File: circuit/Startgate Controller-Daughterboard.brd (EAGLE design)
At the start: 70 x 90 mm, 14 parts, among them U2 HEF4066BT, U3 HEF4066BT, U4 HEF4066BT, U5 HEF4066BT

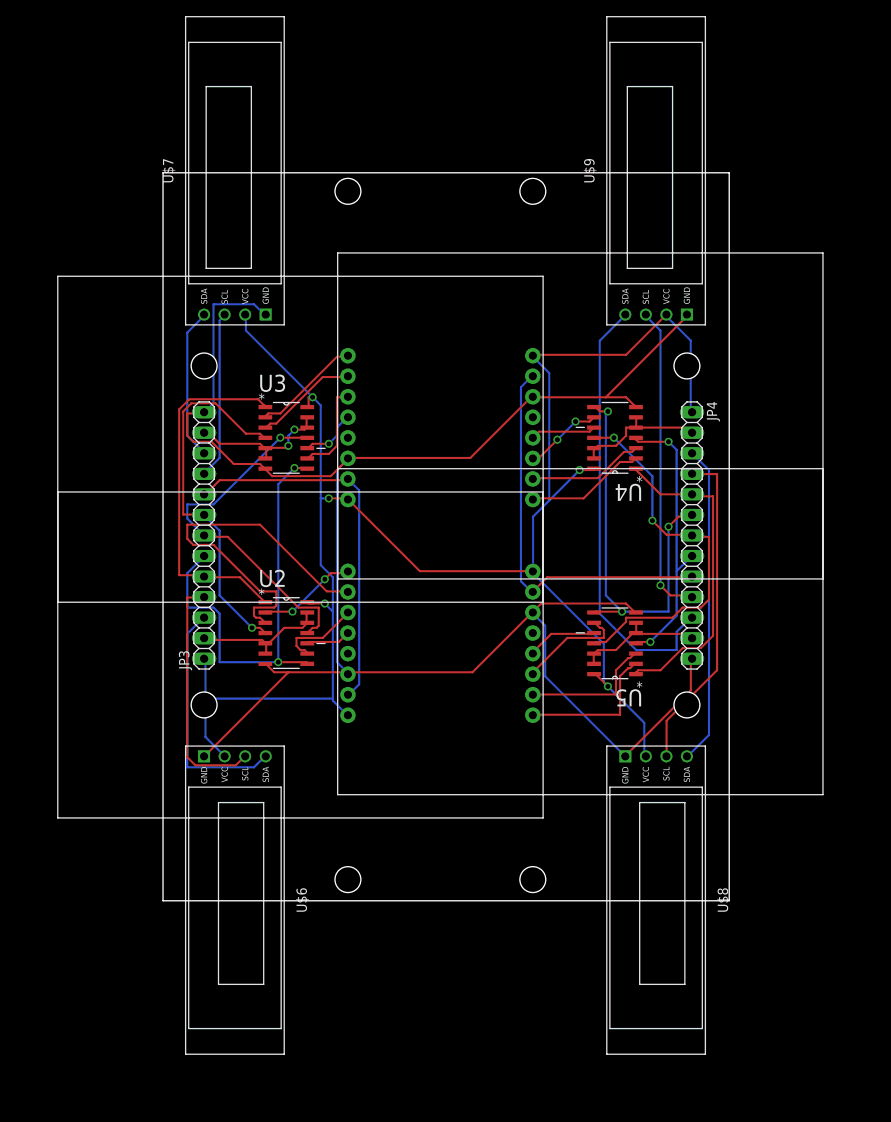
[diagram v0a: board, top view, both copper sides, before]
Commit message: correct some schematics mistakes and add gerber files
A demo mode button was added to the controller, the layout of the
controller shield as well as the startgate displays were changed.
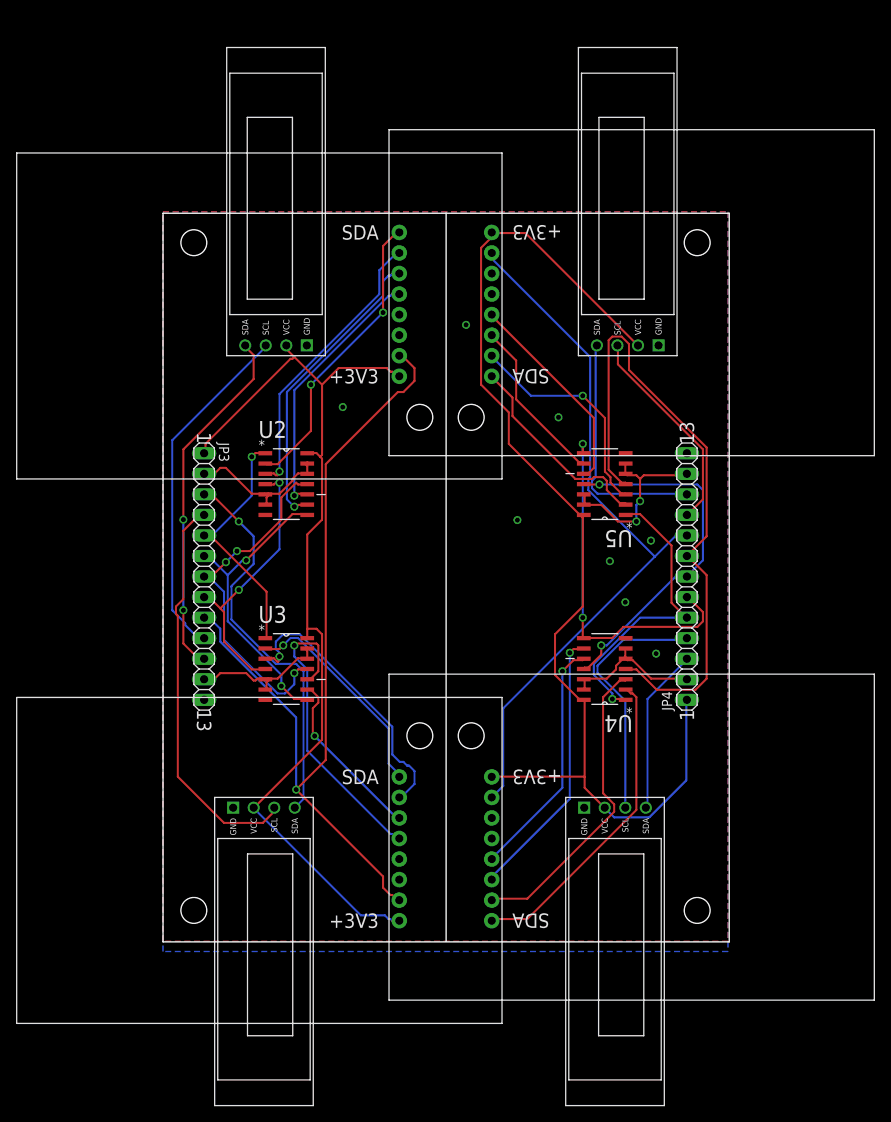
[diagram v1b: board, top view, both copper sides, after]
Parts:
- moved U$3 52.5 mm to (27.9, 33.0)
- moved U$4 52.3 mm to (41.9, -10.2)
- moved U$2 42.4 mm to (27.9, 100.3)
- moved U$5 42.2 mm to (41.9, 57.1)
- moved U4 28.6 mm to (54.6, 33.7)
- moved U3 28.6 mm to (15.2, 33.7)
- moved U5 19.7 mm to (54.6, 56.5)
- moved U2 18.4 mm to (15.2, 56.5)
- moved U$8 8.13 mm to (55.9, -1.27)
- moved U$6 7.29 mm to (12.5, -1.27)
- moved U$7 6.35 mm to (14.0, 91.4)
- moved U$9 5.18 mm to (57.5, 91.4)
- moved JP4 5.12 mm to (64.8, 45.1), turned to 90 degrees
- moved JP3 5.08 mm to (5.08, 45.1), turned to 270 degrees
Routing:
- net GND: track 233.2 -> 0.28 mm, vias 0 -> 8
- net N$16: track 46.5 -> 106.7 mm, vias 0 -> 1
- net SCK: track 35.4 -> 81.0 mm, vias 2 -> 0
- net +3V3: track 217.6 -> 258.7 mm, vias 5 -> 0
- net RST: track 48.5 -> 89.3 mm
- net MISO-OUT2: track 7.17 -> 37.8 mm
- net MISO-OUT1: track 5.55 -> 32.7 mm, vias 0 -> 1
- net MOSI-OUT1: track 10.4 -> 37.3 mm, vias 0 -> 1
- net SDA2: track 18.8 -> 44.3 mm, vias 0 -> 2
- net SDA4: track 54.5 -> 30.0 mm
- net MOSI-OUT3: track 9.68 -> 34.1 mm, vias 2 -> 1
- net SS-OUT1: track 12.4 -> 36.7 mm
- net SS-OUT3: track 14.9 -> 39.3 mm
- net SCK-OUT3: track 14.4 -> 38.2 mm
- net SCK-OUT2: track 12.8 -> 35.4 mm, vias 0 -> 1
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- added copper zone on layer 1, net GND
- added copper zone on layer 16, net GND
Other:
- board size 70 x 90 mm -> 70 x 90.1 mm
- board text added: "+3V3"
- board text added: "1"
- board text added: "13"
- board text added: "SDA"
